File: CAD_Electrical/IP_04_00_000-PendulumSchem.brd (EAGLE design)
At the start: 160 x 100 mm, 7 parts

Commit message: Changed size of pcb board
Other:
- board size 160 x 100 mm -> 101.6 x 55.5 mm
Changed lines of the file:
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@@
 <board>
 <plain>
-<wire x1="0" y1="0" x2="160" y2="0" width="0" layer="20"/>
-<wire x1="160" y1="0" x2="160" y2="100" width="0" layer="20"/>
-<wire x1="160" y1="100" x2="0" y2="100" width="0" layer="20"/>
-<wire x1="0" y1="100" x2="0" y2="0" width="0" layer="20"/>
+<wire x1="0" y1="0" x2="101.58" y2="0" width="0" layer="20"/>
+<wire x1="101.58" y1="0" x2="101.58" y2="55.55" width="0" layer="20"/>
+<wire x1="101.58" y1="55.55" x2="0" y2="55.55" width="0" layer="20"/>
+<wire x1="0" y1="55.55" x2="0" y2="0" width="0" layer="20"/>
 </plain>
 <attributes>

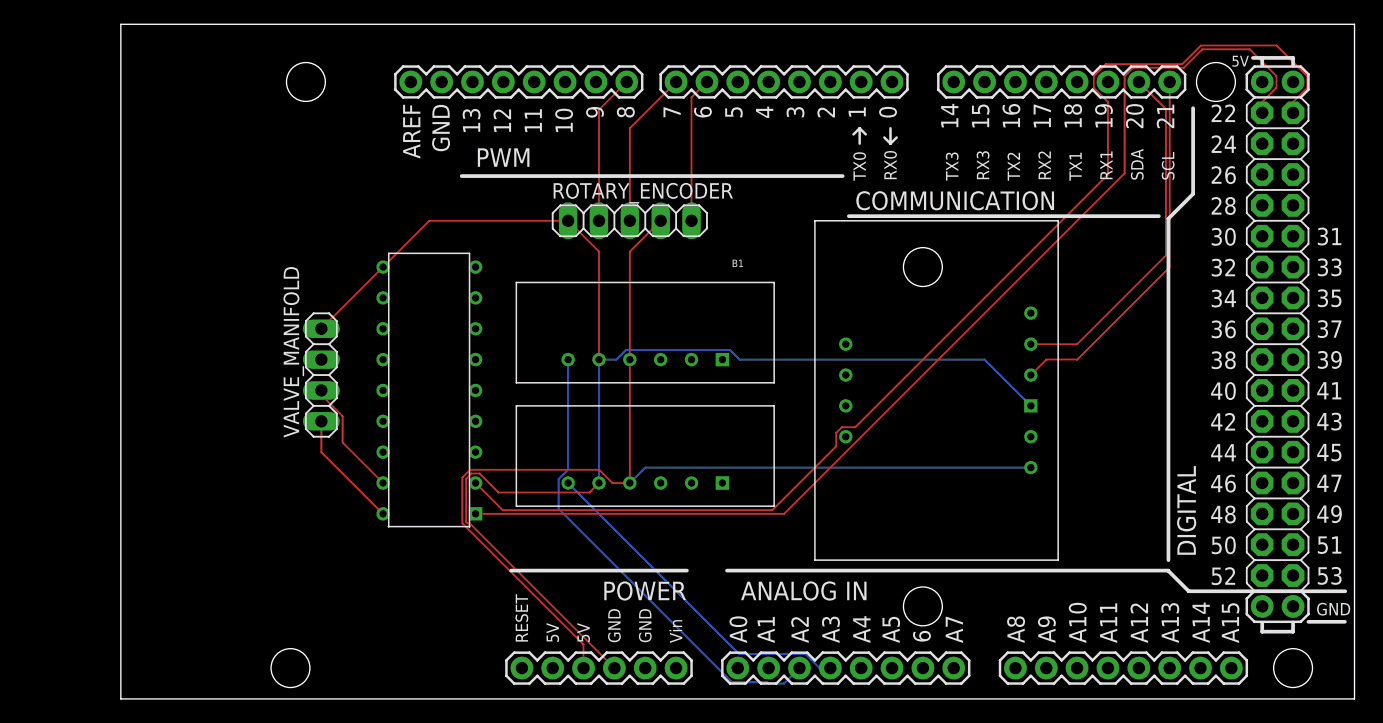
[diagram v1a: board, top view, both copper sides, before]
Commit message: Fixed encoder routing to interrupt & created ground plane
Also inserted text, fixed footprints of custom devices, and replaced standard pins with screw terminals for more secure connection
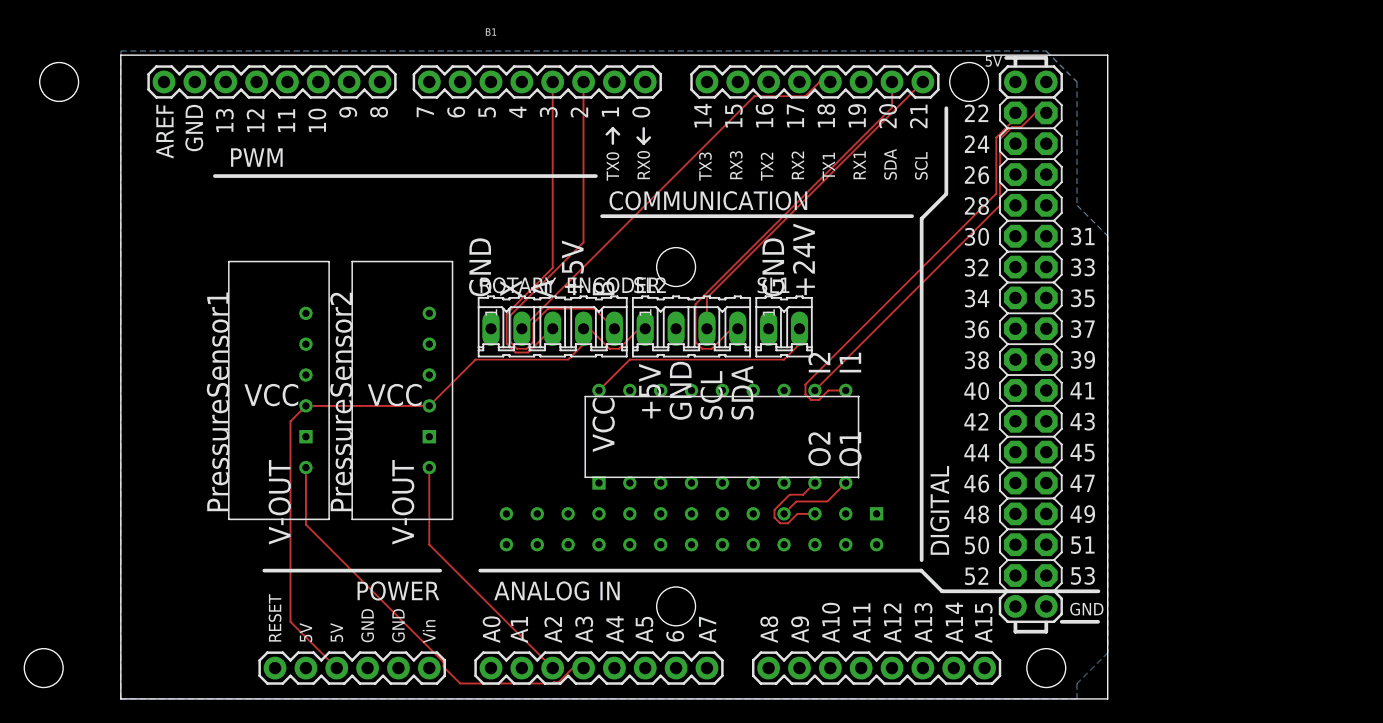
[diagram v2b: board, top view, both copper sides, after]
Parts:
- removed U$1: IMU, IPcustomDevices:IMU
- removed VALVE_MANIFOLD: (no value), pinhead:1X04
- added SL1: (no value), con-amp-quick:02P
- added SL2: (no value), con-amp-quick:04P
- added U$5: VALVE_MANIFOLD, IPcustomDevices:VALVE_MANIFOLD
- ROTARY_ENCODER: device pinhead:1X05 -> con-amp-quick:05P
- moved U$2 32.1 mm to (59.7, 25.4), turned to 270 degrees
- moved U$4 21.6 mm to (15.2, 19.1), turned to 0 degrees
- moved B1 20.3 mm to (29.2, 26.7)
- moved U$3 14.5 mm to (25.4, 19.1), turned to 0 degrees
- moved ROTARY_ENCODER 10.9 mm to (35.6, 30.5)
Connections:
- removed net N$11: B1.8, ROTARY_ENCODER.2
- removed net N$9: B1.6, ROTARY_ENCODER.5
- new net N$2: B1.20, SL2.4
- new net N$4: B1.2, ROTARY_ENCODER.5
- net +24V: now also SL1.2
- net +5V: now also SL2.1; no longer U$1.VIN
- net GND: now also SL1.1, SL2.2, U$5.P$1; no longer U$1.GND, VALVE_MANIFOLD.4
- net N$1: now also B1.3; no longer B1.7
- net N$3: now also B1.21, SL2.3; no longer B1.20, U$1.SDA
- net N$6: now also U$5.P$4; no longer VALVE_MANIFOLD.1
- net N$7: now also B1.18, ROTARY_ENCODER.2; no longer B1.21, U$1.SCL
- net N$8: now also U$5.P$3; no longer VALVE_MANIFOLD.2
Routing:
- net GND: track 117.3 -> 0.16 mm
- net N$10: track 96.8 -> 31.7 mm
- net N$5: track 90.9 -> 34.2 mm
- net N$4: track 0.00 -> 35.7 mm
- net +5V: track 90.5 -> 56.4 mm
- net N$2: track 0.00 -> 32.5 mm
- net +24V: track 0.00 -> 19.4 mm
- net N$12: track 38.9 -> 20.7 mm
- net N$1: track 13.0 -> 28.0 mm
- net N$11: track 12.4 -> 0.00 mm
- net N$9: track 12.0 -> 0.00 mm
- net N$14: track 27.9 -> 33.7 mm
- net N$6: track 9.72 -> 6.13 mm
- net N$7: track 30.4 -> 33.8 mm
- net N$3: track 29.4 -> 27.7 mm
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- added copper zone on layer 16, net GND
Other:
- board size 101.6 x 55.5 mm -> 81.3 x 53 mm
- board text added: "+24V"
- board text added: "+5V"
- board text added: "A"
- board text added: "B"
- board text added: "GND"
- board text added: "I1"
- board text added: "I2"
- board text added: "O1"
- board text added: "O2"
- board text added: "PressureSensor1"
- board text added: "PressureSensor2"
- board text added: "SCL"
- board text added: "SDA"
- board text added: "V-OUT"
- board text added: "VCC"
- board text added: "X"

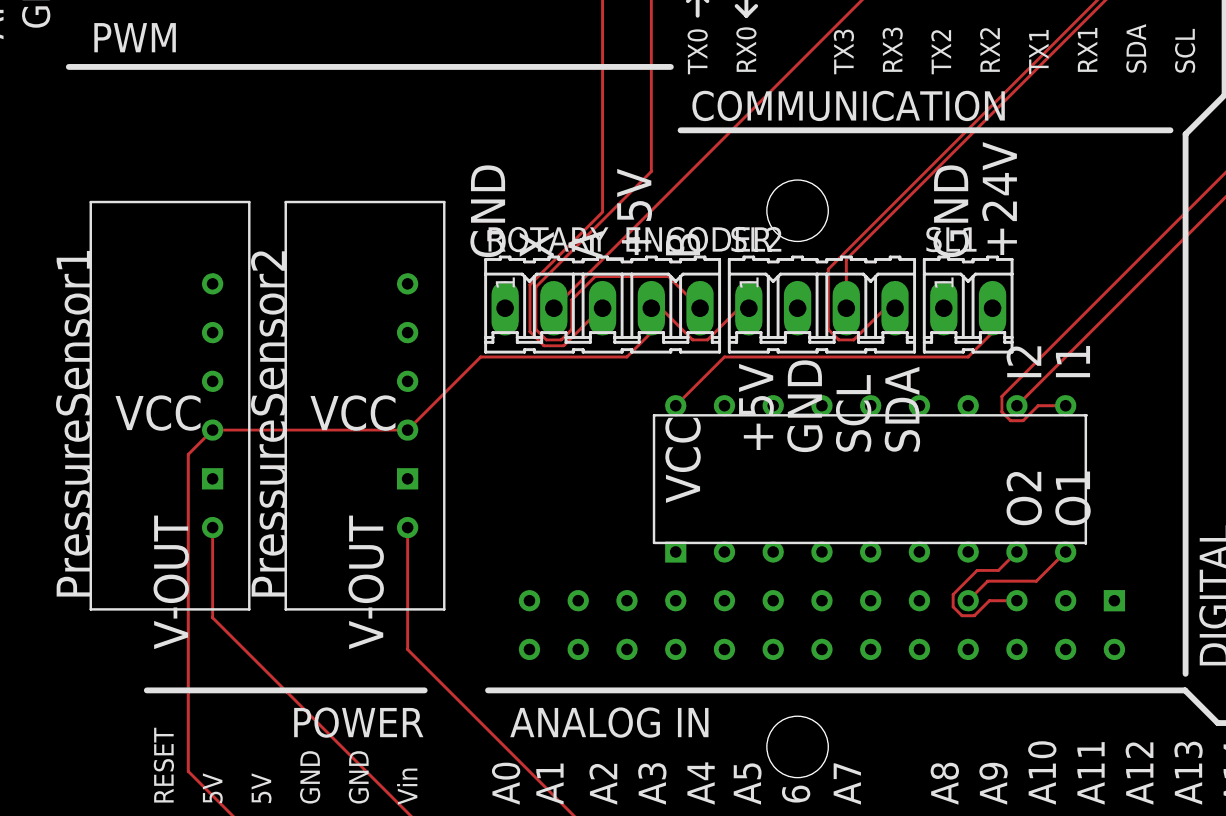
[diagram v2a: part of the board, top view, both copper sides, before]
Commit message: Updated silkscreen to only part names plus external wires
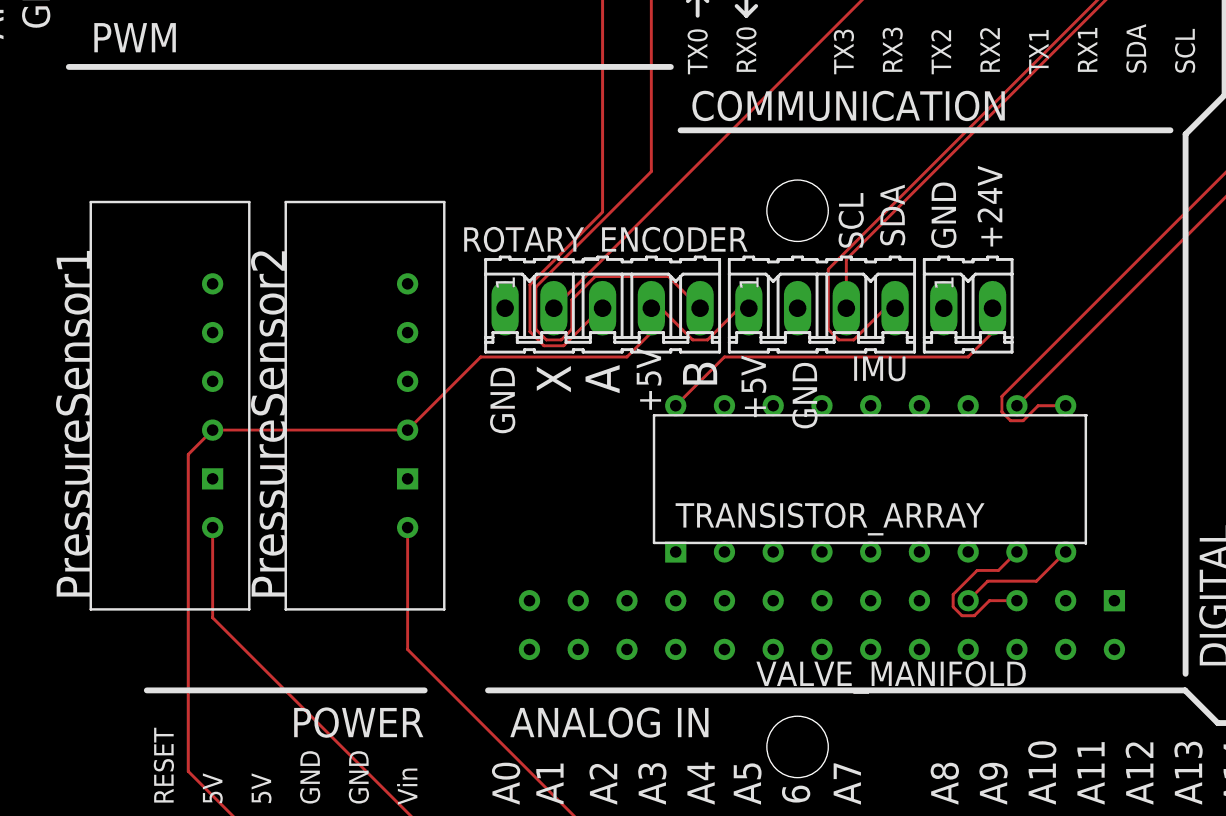
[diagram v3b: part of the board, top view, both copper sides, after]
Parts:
- renumbered SL2 to IMU
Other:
- board text added: "TRANSISTOR_ARRAY"
- board text added: "VALVE_MANIFOLD"
- board text removed: "I1"
- board text removed: "I2"
- board text removed: "O1"
- board text removed: "O2"
- board text removed: "V-OUT"
- board text removed: "VCC"
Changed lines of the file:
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@@
 <text x="8.89" y="15.24" size="1.778" layer="21" rot="R90">PressureSensor1</text>
 <text x="19.05" y="15.24" size="1.778" layer="21" rot="R90">PressureSensor2</text>
-<text x="30.48" y="33.02" size="1.778" layer="21" rot="R90">GND</text>
-<text x="33.02" y="33.02" size="1.778" layer="21" rot="R90">X</text>
-<text x="35.56" y="33.02" size="1.778" layer="21" rot="R90">A</text>
-<text x="38.1" y="33.02" size="1.778" layer="21" rot="R90">+5V</text>
-<text x="40.64" y="33.02" size="1.778" layer="21" rot="R90">B</text>
-<text x="44.45" y="22.86" size="1.778" layer="21" rot="R90">+5V</text>
-<text x="46.99" y="22.86" size="1.778" layer="21" rot="R90">GND</text>
-<text x="49.53" y="22.86" size="1.778" layer="21" rot="R90">SCL</text>
-<text x="52.07" y="22.86" size="1.778" layer="21" rot="R90">SDA</text>
-<text x="40.64" y="20.32" size="1.778" layer="21" rot="R90">VCC</text>
-<text x="60.96" y="19.05" size="1.778" layer="21" rot="R90">O1</text>
-<text x="58.42" y="19.05" size="1.778" layer="21" rot="R90">O2</text>
-<text x="60.96" y="26.67" size="1.778" layer="21" rot="R90">I1</text>
-<text x="58.42" y="26.67" size="1.778" layer="21" rot="R90">I2</text>
-<text x="57.15" y="33.02" size="1.778" layer="21" rot="R90">+24V</text>
-<text x="54.61" y="33.02" size="1.778" layer="21" rot="R90">GND</text>
-<text x="20.32" y="24.13" size="1.778" layer="21">VCC</text>
-<text x="10.16" y="24.13" size="1.778" layer="21">VCC</text>
-<text x="24.13" y="12.7" size="1.778" layer="21" rot="R90">V-OUT</text>
-<text x="13.97" y="12.7" size="1.778" layer="21" rot="R90">V-OUT</text>
+<text x="33.909" y="26.035" size="1.778" layer="21" rot="R90">X</text>
+<text x="36.449" y="26.035" size="1.778" layer="21" rot="R90">A</text>
+<text x="41.529" y="26.289" size="1.778" layer="21" rot="R90">B</text>
+<text x="56.388" y="33.528" size="1.27" layer="21" rot="R90">+24V</text>
+<text x="53.975" y="33.528" size="1.27" layer="21" rot="R90">GND</text>
+<text x="39.37" y="19.05" size="1.27" layer="21">TRANSISTOR_ARRAY</text>
+<text x="43.561" y="10.795" size="1.27" layer="21">VALVE_MANIFOLD</text>
+<text x="49.149" y="33.528" size="1.27" layer="21" rot="R90">SCL</text>
+<text x="51.308" y="33.655" size="1.27" layer="21" rot="R90">SDA</text>
+<text x="38.608" y="25.019" size="1.27" layer="21" rot="R90">+5V</text>
+<text x="30.988" y="23.876" size="1.27" layer="21" rot="R90">GND</text>
+<text x="44.069" y="24.638" size="1.27" layer="21" rot="R90">+5V</text>
+<text x="46.736" y="24.13" size="1.27" layer="21" rot="R90">GND</text>
 </plain>
 <attributes>
@@
 <attribute name="MF" value="" x="123.19" y="-30.48" size="1.778" layer="27" display="off"/>
 <attribute name="MPN" value="" x="123.19" y="-30.48" size="1.778" layer="27" display="off"/>
-<attribute name="NAME" x="29.464" y="33.4264" size="1.27" layer="25" ratio="10"/>
+<attribute name="NAME" x="28.194" y="33.4264" size="1.27" layer="25" ratio="10"/>
 <attribute name="OC_FARNELL" value="unknown" x="123.19" y="-30.48" size="1.778" layer="27" display="off"/>
 <attribute name="OC_NEWARK" value="unknown" x="123.19" y="-30.48" size="1.778" layer="27" display="off"/>
@@
 <attribute name="MF" value="" x="152.4" y="-30.48" size="1.778" layer="27" display="off"/>
 <attribute name="MPN" value="" x="152.4" y="-30.48" size="1.778" layer="27" display="off"/>
-<attribute name="NAME" x="52.324" y="33.4264" size="1.27" layer="25" ratio="10"/>
 <attribute name="OC_FARNELL" value="unknown" x="152.4" y="-30.48" size="1.778" layer="27" display="off"/>
 <attribute name="OC_NEWARK" value="unknown" x="152.4" y="-30.48" size="1.778" layer="27" display="off"/>
@@
 <element name="U$4" library="IPcustomDevices" package="PRESSURE_SENSOR" value="PRESSURE_SENSOR" x="15.24" y="19.05" smashed="yes"/>
 <element name="U$5" library="IPcustomDevices" package="VALVE_MANIFOLD" value="VALVE_MANIFOLD" x="62.23" y="15.24" smashed="yes" rot="MR270"/>
-<element name="SL2" library="con-amp-quick" library_urn="urn:adsk.eagle:library:125" package="04P" package3d_urn="urn:adsk.eagle:package:5958/1" value="" x="46.99" y="30.48" smashed="yes">
+<element name="IMU" library="con-amp-quick" library_urn="urn:adsk.eagle:library:125" package="04P" package3d_urn="urn:adsk.eagle:package:5958/1" value="" x="46.99" y="30.48" smashed="yes">
 <attribute name="MF" value="" x="46.99" y="30.48" size="1.778" layer="27" display="off"/>
 <attribute name="MPN" value="" x="46.99" y="30.48" size="1.778" layer="27" display="off"/>
-<attribute name="NAME" x="42.164" y="33.4264" size="1.27" layer="25" ratio="10"/>
+<attribute name="NAME" x="48.514" y="26.6954" size="1.27" layer="25" ratio="10"/>
 <attribute name="OC_FARNELL" value="unknown" x="46.99" y="30.48" size="1.778" layer="27" display="off"/>
 <attribute name="OC_NEWARK" value="unknown" x="46.99" y="30.48" size="1.778" layer="27" display="off"/>
@@
 <contactref element="U$4" pad="P$2"/>
 <contactref element="SL1" pad="1"/>
-<contactref element="SL2" pad="2"/>
+<contactref element="IMU" pad="2"/>
 <wire x1="15.24" y1="21.59" x2="15.24" y2="21.75323125" width="0.1524" layer="16"/>
 <polygon width="0.1524" layer="16">
@@
 <contactref element="U$3" pad="P$3"/>
 <contactref element="U$4" pad="P$3"/>
-<contactref element="SL2" pad="1"/>
+<contactref element="IMU" pad="1"/>
 <wire x1="15.24" y1="24.13" x2="13.97" y2="22.86" width="0.1524" layer="1"/>
 <wire x1="13.97" y1="22.86" x2="13.97" y2="6.35" width="0.1524" layer="1"/>
@@
 <signal name="N$2">
 <contactref element="B1" pad="20"/>
-<contactref element="SL2" pad="4"/>
+<contactref element="IMU" pad="4"/>
 <wire x1="48.64928125" y1="28.829" x2="47.87071875" y2="28.829" width="0.1524" layer="1"/>
 <wire x1="47.87071875" y1="28.829" x2="47.3202" y2="29.37951875" width="0.1524" layer="1"/>
@@
 <signal name="N$3">
 <contactref element="B1" pad="21"/>
-<contactref element="SL2" pad="3"/>
+<contactref element="IMU" pad="3"/>
 <wire x1="48.26" y1="30.48" x2="48.26" y2="33.02" width="0.1524" layer="1"/>
 <wire x1="48.26" y1="33.02" x2="66.04" y2="50.8" width="0.1524" layer="1"/>

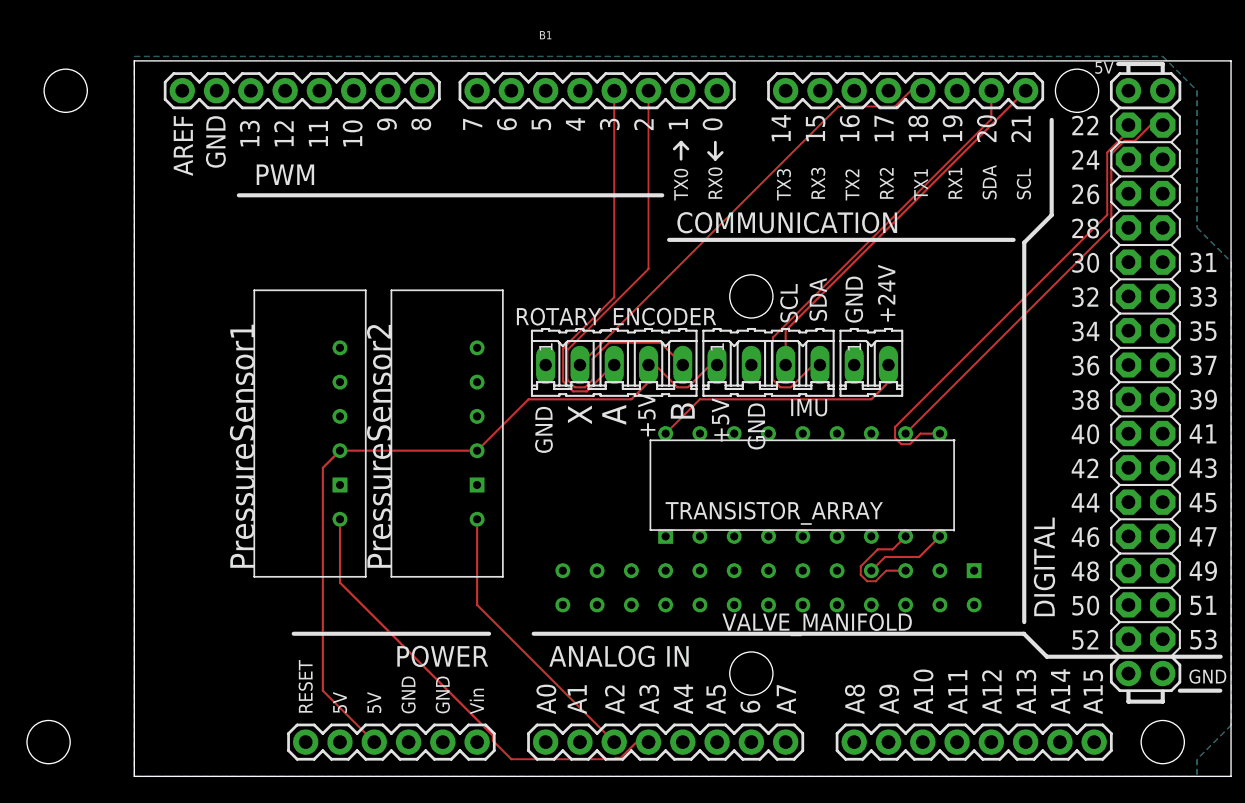
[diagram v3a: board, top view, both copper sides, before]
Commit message: Widened 24V connection & Deleted extraneous holes & MicroSD added
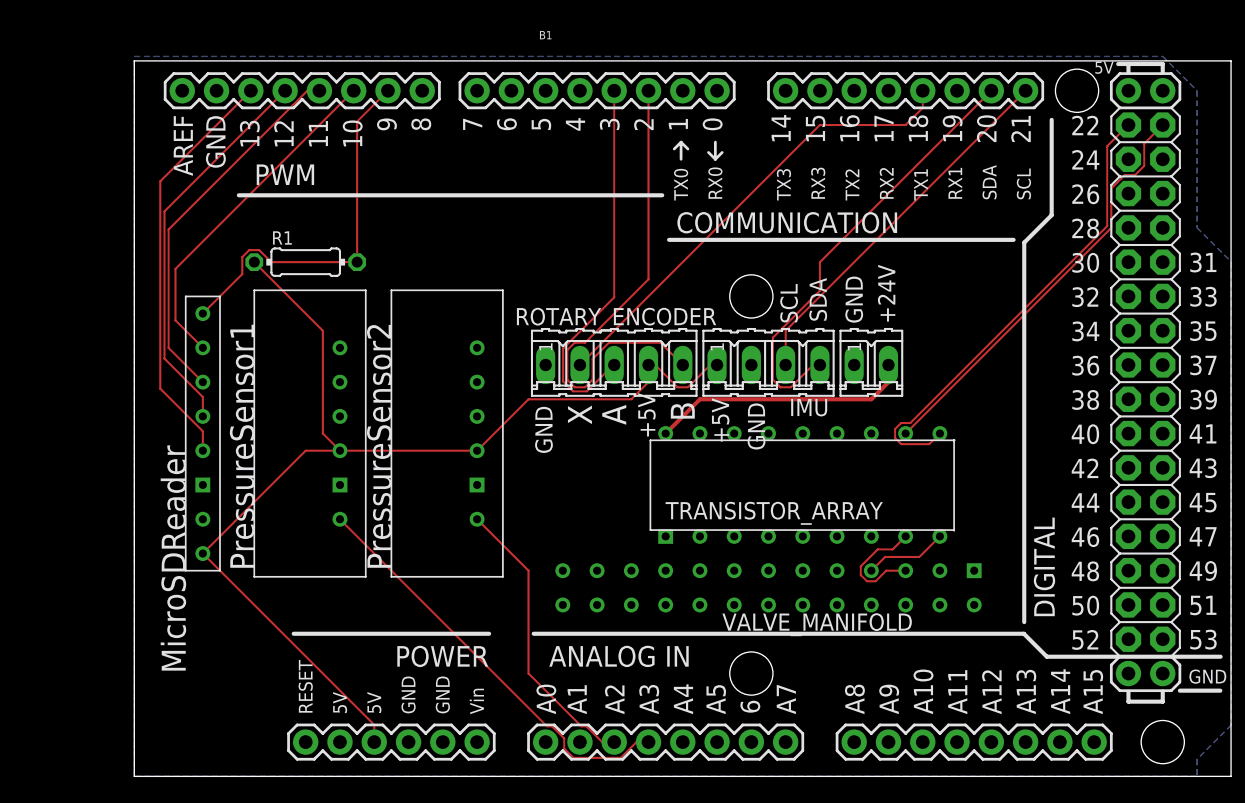
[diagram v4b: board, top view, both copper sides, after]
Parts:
- added R1: (no value), rcl:0204/7
- added U$1: MICROSD_READER, IPcustomDevices:MICROSD_READER
- B1: device SparkFun-Boards:ARDUINO_MEGA -> SparkFun-Boards-deleted2holes:ARDUINO_MEGA
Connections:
- new net N$11: B1.13, U$1.CLK
- new net N$13: B1.12, U$1.DO
- new net N$15: B1.11, U$1.DI
- new net N$16: B1.10, U$1.CS
- new net N$18: B1.9, R1.2, U$1.CD
- net +5V: now also R1.1, U$1.5V
- net GND: now also U$1.GND
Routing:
- net N$11: track 0.00 -> 30.8 mm
- net N$13: track 0.00 -> 29.0 mm
- net N$18: track 0.00 -> 28.1 mm
- net N$15: track 0.00 -> 27.8 mm
- net N$16: track 0.00 -> 25.5 mm
- net +5V: track 56.4 -> 81.8 mm
- net N$14: track 33.7 -> 31.1 mm
- net N$7: track 33.8 -> 34.6 mm
- net N$12: track 20.7 -> 21.5 mm
- net N$10: track 31.7 -> 31.2 mm
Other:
- board text added: "MicroSDReader"
